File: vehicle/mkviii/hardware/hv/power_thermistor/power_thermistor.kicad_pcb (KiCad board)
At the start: 4 copper layers, 401 x 176.1 mm, 97 parts, among them J10 Battery Cell Spot Weld, J11 Battery Cell Spot Weld, J12 Battery Cell Spot Weld, J13 Battery Cell Spot Weld, J14 Battery Cell Spot Weld, J15 Battery Cell Spot Weld, J16 Battery Cell Spot Weld, J17 Battery Cell Spot Weld, J18 Battery Cell Spot Weld, J19 Battery Cell Spot Weld, J2 43045-02YY_121314, J2 EHT-110-01-F-D, J20 Battery Cell Spot Weld, J3 EHT-110-01-F-D, J5 Battery Cell Spot Weld, J6 Battery Cell Spot Weld, J6 EHT-110-01-F-D, J7 Battery Cell Spot Weld, J8 Battery Cell Spot Weld, J9 Battery Cell Spot Weld

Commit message: Added Production Files and updated PCB file to match PCB file used for production files.
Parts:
- added kibuzzard-69840B33: G***, kibuzzard-69840B33, F.Cu at (71.2, 32.4)
- added kibuzzard-69840B56: G***, kibuzzard-69840B56, F.Cu at (74.3, 35.2)
- added kibuzzard-69840BF2: G***, kibuzzard-69840BF2, F.Cu at (224.3, 35.0)
- added kibuzzard-69840BF7: G***, kibuzzard-69840BF7, F.Cu at (224.1, 37.6)
- added kibuzzard-69840C1E: G***, kibuzzard-69840C1E, F.Cu at (297.1, 37.8)
- added kibuzzard-69840C4F: G***, kibuzzard-69840C4F, F.Cu at (298.9, 35.2)
- added kibuzzard-69840C62: G***, kibuzzard-69840C62, F.Cu at (342.2, 37.8)
- added kibuzzard-69840C71: G***, kibuzzard-69840C71, F.Cu at (343.5, 35.2)
- moved kibuzzard-6738FB72 2.18 mm to (327.2, 36.5)
- moved kibuzzard-6738FB72 0.67 mm to (282.6, 36.5)
- moved kibuzzard-6738FA22 0.35 mm to (210.4, 36.5)
- renumbered REF** to U1
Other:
- board text removed: "02/2026"
- board text removed: "Liam Fries"

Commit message: Power Therm overhall, have not been reviewed yet
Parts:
- removed the J2 at (185.0, 27.7)
- removed the J2 at (216.2, 29.1)
- added J1: T2M-110-01-X-D-TH-WT, OEM:SAMTEC_EHT-110-01-X-D (J_EHT-110-01-F-D), B.Cu at (290.3, 29.0)
- added J2: J_Molex_Header_01x02_VT, OEM:J_Molex_Header_01x02_VT - 43045-02YY_121314, B.Cu at (161.9, 30.4)
- added J20: Battery Cell Spot Weld, OEM:J_Bond_Pad_4p, F.Cu at (-10.3, 26.7)
- added J23: Battery Cell Spot Weld, OEM:J_Bond_Pad_4p, F.Cu at (-0.81, 26.7)
- added J4: T2M-110-01-X-D-TH-WT, OEM:SAMTEC_EHT-110-01-X-D (J_EHT-110-01-F-D), B.Cu at (216.1, 29.0)
- added kibuzzard-6738FA22: G***, kibuzzard-6738FA22, F.Cu at (210.4, 36.5)
- added kibuzzard-6738FB72: G***, kibuzzard-6738FB72, B.Cu at (298.3, 36.4)
- added kibuzzard-6738FB72: G***, kibuzzard-6738FB72, B.Cu at (345.5, 36.5)
- added kibuzzard-69840BF2: G***, kibuzzard-69840BF2, F.Cu at (224.3, 35.0)
- added kibuzzard-69840BF7: G***, kibuzzard-69840BF7, F.Cu at (224.1, 37.6)
- added kibuzzard-69840C1E: G***, kibuzzard-69840C1E, B.Cu at (283.9, 37.8)
- added kibuzzard-69840C4F: G***, kibuzzard-69840C4F, B.Cu at (282.0, 35.2)
- added kibuzzard-69840C62: G***, kibuzzard-69840C62, B.Cu at (330.6, 37.9)
- added kibuzzard-69840C71: G***, kibuzzard-69840C71, B.Cu at (329.3, 35.3)
- J19: renamed from J2; value (none) -> Battery Cell Spot Weld
- J3: value EHT-110-01-F-D -> T2M-110-01-X-D-TH-WT; moved to B.Cu
- J6: value EHT-110-01-F-D -> J_Molex_Header_01x02_VT; footprint OEM:SAMTEC_EHT-110-01-X-D (J_EHT-110-01-F-D) -> OEM:J_Molex_Header_01x02_VT - 43045-02YY_121314; moved to B.Cu
- REF** (x2), kibuzzard-6738FA22, kibuzzard-69840BF2, kibuzzard-69840BF7: moved to B.Cu
- U1: value 21-0036K_MXM -> DS18B20U
- moved TH1 319.3 mm to (56.4, 106.0)
- moved TH2 319.3 mm to (56.4, 159.7)
- moved J6 75.0 mm to (365.2, 30.4)
- moved TH18 24.0 mm to (229.6, 160.0), turned to 90 degrees
- moved TH21 21.8 mm to (270.0, 105.9)
- moved TH22 21.8 mm to (270.0, 159.8)
- moved TH10 21.7 mm to (142.0, 159.8)
- moved TH9 21.7 mm to (142.0, 105.9)
- moved TH3 21.5 mm to (77.9, 92.5)
- moved TH4 21.5 mm to (77.9, 146.4)
- moved TH19 21.5 mm to (248.4, 92.4)
- moved TH27 21.4 mm to (333.6, 92.5)
- moved TH28 21.4 mm to (333.6, 146.4)
- moved TH23 21.3 mm to (290.8, 92.5)
- moved TH24 21.3 mm to (290.8, 146.4)
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- renumbered J12 to J10, J13 to J11, J14 to J12, J15 to J13, J16 to J14, J17 to J15, J18 to J16, J19 to J17, J7 to J18, J20 to J22, J8 to J5, J9 to J50, J6 to J51, J5 to J7, J10 to J8, J11 to J9, TH31 to TH1, TH8 to TH10, TH9 to TH11, TH10 to TH12, TH11 to TH13, TH12 to TH14, TH13 to TH15, TH14 to TH16, TH15 to TH17, TH16 to TH18, TH17 to TH19, TH32 to TH2, TH18 to TH20, TH19 to TH21, TH20 to TH22, TH21 to TH23, TH22 to TH24, TH23 to TH25, TH24 to TH26, TH25 to TH27, TH26 to TH28, TH27 to TH29, TH1 to TH3, TH28 to TH30, TH29 to TH31, TH30 to TH32, TH2 to TH4, TH3 to TH5, TH4 to TH6, TH5 to TH7, TH6 to TH8, TH7 to TH9
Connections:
- F5 pad 1: Net-(JP1-B) -> Net-(JP9-B)
- J3 pad 01: Therm18 -> GND
- J3 pad 02: unconnected-(J3-Pad02) -> Therm17
- J3 pad 03: Therm19 -> Therm31
- J3 pad 04: Therm17 -> Therm18
- J3 pad 05: GND -> Therm32
- J3 pad 06: Therm32 -> GND
- J3 pad 07: Therm20 -> Therm29
- J3 pad 08: Therm31 -> Therm20
- J3 pad 09: Therm21 -> GND
- J3 pad 10: GND -> Therm19
- J3 pad 11: Therm22 -> Therm30
- J3 pad 12: Therm30 -> Therm22
- J3 pad 13: Therm23 -> Therm27
- J3 pad 14: Therm29 -> Therm21
- J3 pad 15: GND -> Therm28
- J3 pad 16: Therm28 -> GND
- J3 pad 17: Therm24 -> Therm25
- J3 pad 18: Therm27 -> Therm24
- J3 pad 19: Therm25 -> Therm26
- J3 pad 20: Therm26 -> Therm23
- JP9 pad 2: Net-(JP1-B) -> Net-(JP9-B)
- TH1 pad 2: Therm31 -> Therm1
- TH10 pad 2: Therm8 -> Therm10
- TH11 pad 2: Therm9 -> Therm11
- TH12 pad 2: Therm10 -> Therm12
- TH13 pad 2: Therm11 -> Therm13
- TH14 pad 2: Therm12 -> Therm14
- TH15 pad 2: Therm13 -> Therm15
- TH16 pad 2: Therm14 -> Therm16
- TH17 pad 2: Therm15 -> Therm17
- TH18 pad 2: Therm16 -> Therm18
- TH19 pad 2: Therm17 -> Therm19
- TH2 pad 2: Therm32 -> Therm2
- TH20 pad 2: Therm18 -> Therm20
- TH21 pad 2: Therm19 -> Therm21
- TH22 pad 2: Therm20 -> Therm22
- TH23 pad 2: Therm21 -> Therm23
- TH24 pad 2: Therm22 -> Therm24
- TH25 pad 2: Therm23 -> Therm25
- TH26 pad 2: Therm24 -> Therm26
- TH27 pad 2: Therm25 -> Therm27
- TH28 pad 2: Therm26 -> Therm28
- TH29 pad 2: Therm27 -> Therm29
- TH3 pad 2: Therm1 -> Therm3
- TH30 pad 2: Therm28 -> Therm30
- TH31 pad 2: Therm29 -> Therm31
- TH32 pad 2: Therm30 -> Therm32
- TH4 pad 2: Therm2 -> Therm4
- TH5 pad 2: Therm3 -> Therm5
- TH6 pad 2: Therm4 -> Therm6
- TH7 pad 2: Therm5 -> Therm7
- TH8 pad 2: Therm6 -> Therm8
- TH9 pad 2: Therm7 -> Therm9
- U1 pad 1: unconnected-(J2-Pad18) -> Net-(U1-DQ)
- U1 pad 2: (no net) -> unconnected-(U1-NC-Pad2)
- U1 pad 3: (no net) -> unconnected-(U1-NC-Pad3)
- U1 pad 4: unconnected-(J2-Pad19) -> Net-(U1-GND)
- U1 pad 5: (no net) -> unconnected-(U1-NC-Pad5)
- U1 pad 6: (no net) -> unconnected-(U1-NC-Pad6)
- U1 pad 7: (no net) -> unconnected-(U1-NC-Pad7)
- U1 pad 8: unconnected-(J2-Pad19) -> Net-(U1-GND)
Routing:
- net Net-(U1-GND): track 0.00 -> 365.0 mm, vias 0 -> 2
- net Net-(U1-DQ): track 0.00 -> 333.6 mm, vias 0 -> 3
- net unconnected-(J2-Pad18): track 164.5 -> 0.00 mm, vias 2 -> 0
- net unconnected-(J2-Pad19): track 152.8 -> 0.00 mm, vias 2 -> 0
- net Therm15: track 227.3 -> 150.8 mm
- net Therm11: track 254.2 -> 181.5 mm
- net Therm12: track 294.5 -> 240.5 mm
- net Therm16: track 267.4 -> 216.3 mm
- net Therm9: track 254.8 -> 206.0 mm
- net Therm13: track 226.1 -> 177.9 mm
- net CELL4: track 197.4 -> 154.5 mm
- net CELL5: track 173.4 -> 132.4 mm
- net CELL3: track 221.5 -> 181.0 mm
- net Therm14: track 268.9 -> 232.2 mm
- net CELL6: track 149.1 -> 114.4 mm
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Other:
- board size 401 x 176.1 mm -> 400.9 x 174.3 mm

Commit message: fixed suggested edits and moved connector
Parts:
- removed J20, J23: Battery Cell Spot Weld, OEM:J_Bond_Pad_4p
- removed kibuzzard-69840B33: G***, kibuzzard-69840B33
- removed kibuzzard-69840B56: G***, kibuzzard-69840B56
- added kibuzzard-69DFA9BC: G***, kibuzzard-69DFA9BC, F.Cu at (79.0, 35.2)
- added kibuzzard-69DFAA3E: G***, kibuzzard-69DFAA3E, F.Cu at (74.3, 38.1)
- added kibuzzard-69E00A54: G***, kibuzzard-69E00A54, B.Cu at (104.8, 31.9)
- added kibuzzard-69E00A54: G***, kibuzzard-69E00A54, B.Cu at (270.4, 32.2)
- moved J6 95.3 mm to (270.2, 23.6)
- moved J2 57.7 mm to (104.6, 23.6)
- moved J3 9.44 mm to (344.3, 25.3)
- moved kibuzzard-6738FA22 9.44 mm to (229.9, 32.6)
- moved kibuzzard-69840C1E 9.44 mm to (292.5, 34.0)
- moved kibuzzard-69840C4F 9.44 mm to (307.5, 31.4)
- moved kibuzzard-69840C62 9.44 mm to (339.2, 34.1)
- moved kibuzzard-69840C71 9.44 mm to (352.1, 31.4)
- moved kibuzzard-69840C71 9.44 mm to (337.9, 31.5)
- moved kibuzzard-69840C1E 9.44 mm to (305.7, 34.0)
- moved kibuzzard-69840C4F 9.44 mm to (290.7, 31.4)
- moved kibuzzard-69840C62 9.44 mm to (350.8, 34.0)
- moved kibuzzard-6738FA22 9.44 mm to (219.0, 32.6)
- moved kibuzzard-69840BF7 9.44 mm to (232.7, 33.8)
- moved kibuzzard-69840BF7 9.44 mm to (216.2, 33.8)
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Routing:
- net Net-(U1-GND): track 365.0 -> 300.9 mm, vias 2 -> 1
- net Net-(U1-DQ): track 333.6 -> 298.6 mm, vias 3 -> 4
- net Therm18: track 205.1 -> 216.6 mm
- net Therm19: track 139.7 -> 151.2 mm
- net Therm21: track 131.6 -> 142.9 mm
- net Therm22: track 194.1 -> 205.3 mm
- net Therm20: track 197.4 -> 208.6 mm
- net Therm17: track 160.0 -> 171.0 mm
- net CELL16: track 248.3 -> 237.7 mm
- net Therm24: track 169.3 -> 180.0 mm
- net Therm23: track 107.3 -> 117.9 mm
- net Therm10: track 267.9 -> 278.4 mm
- net CELL10: track 120.1 -> 109.8 mm
- net Therm9: track 206.0 -> 216.2 mm
- net CELL5: track 132.4 -> 142.6 mm
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
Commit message: Minor redcube schematic changes; added some silkscreen; added production files
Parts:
- removed kibuzzard-69DFAA3E: G***, kibuzzard-69DFAA3E
- added G***: LOGO, LOGO, B.Cu at (74.1, 37.6)
- added REF**: OEM_Logo_8mm, OEM:OEM_Logo_8mm, B.Cu at (94.4, 24.4)
- added kibuzzard-67390047: G***, kibuzzard-67390047, B.Cu at (82.7, 21.6)
- added kibuzzard-69DFA9BC: G***, kibuzzard-69DFA9BC, B.Cu at (76.4, 24.4)
- added kibuzzard-69E00A54: G***, kibuzzard-69E00A54, F.Cu at (270.4, 32.2)
- added kibuzzard-69E00A54: G***, kibuzzard-69E00A54, F.Cu at (104.8, 31.9)
- added kibuzzard-69E05987: G***, kibuzzard-69E05987, F.Cu at (80.2, 27.3)
- added kibuzzard-69E05987: G***, kibuzzard-69E05987, B.Cu at (81.1, 27.3)
- J20, J23: renamed from REF**; value J_Wurth_7461115 -> J_Redcube
- moved kibuzzard-6739182D 66.3 mm to (174.7, 24.8)
- moved G*** 13.9 mm to (74.4, 37.4)
- moved REF** 12.3 mm to (66.9, 24.4)
- moved kibuzzard-67390047 12.3 mm to (78.7, 21.6)
- moved kibuzzard-69DFA9BC 12.3 mm to (84.9, 24.4)
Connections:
- J1 pad 13: Therm3 -> Therm4
- J1 pad 15: Therm4 -> Therm3
- J4 pad 01: CELL4 -> CELL1
- J4 pad 02: CELL5 -> CELL16
- J4 pad 03: CELL3 -> CELL2
- J4 pad 04: CELL6 -> CELL15
- J4 pad 05: CELL2 -> CELL3
- J4 pad 06: CELL7 -> CELL14
- J4 pad 07: CELL1 -> CELL4
- J4 pad 08: CELL8 -> CELL13
- J4 pad 09: CELL16 -> CELL5
- J4 pad 10: CELL9 -> CELL12
- J4 pad 11: CELL15 -> CELL6
- J4 pad 12: CELL10 -> CELL11
- J4 pad 13: CELL14 -> CELL7
- J4 pad 14: CELL11 -> CELL10
- J4 pad 16: CELL12 -> CELL9
- J4 pad 18: CELL13 -> CELL8
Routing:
- added copper zone on B.Cu, net (none)
- added copper zone on F.Cu, net (none)
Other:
- board text added: "+"
- board text added: "-"
- board text added: "0"
- board text added: "1"
- board text added: "10"
- board text added: "11"
- board text added: "12"
- board text added: "13"
- board text added: "14"
- board text added: "15"
- board text added: "16"
- board text added: "2"
- board text added: "3"
- board text added: "4"
- board text added: "5"
- board text added: "6"
- board text added: "7"
- board text added: "8"
- board text added: "9"

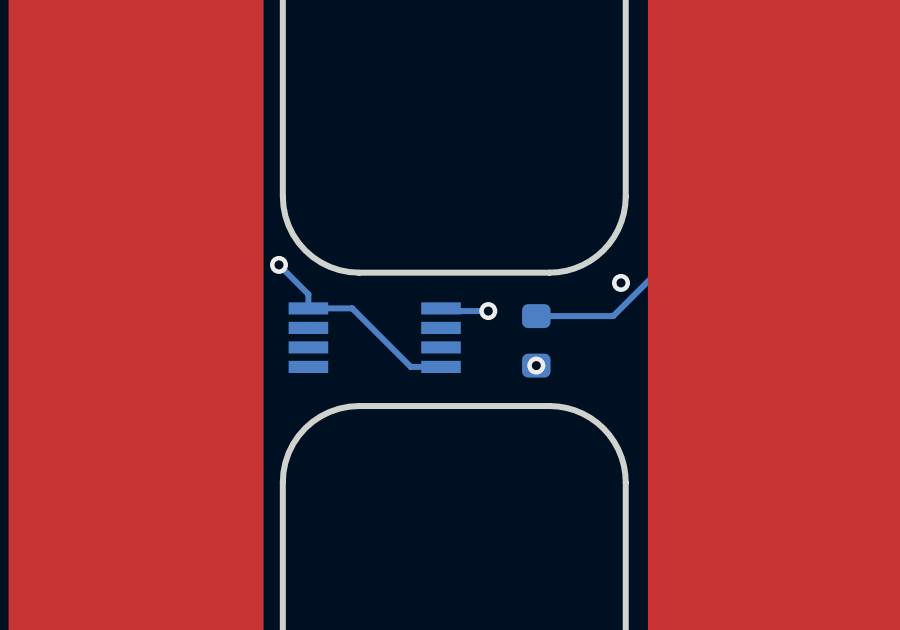
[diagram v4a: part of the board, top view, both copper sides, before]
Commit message: moved e-meter part and moved up GND plane
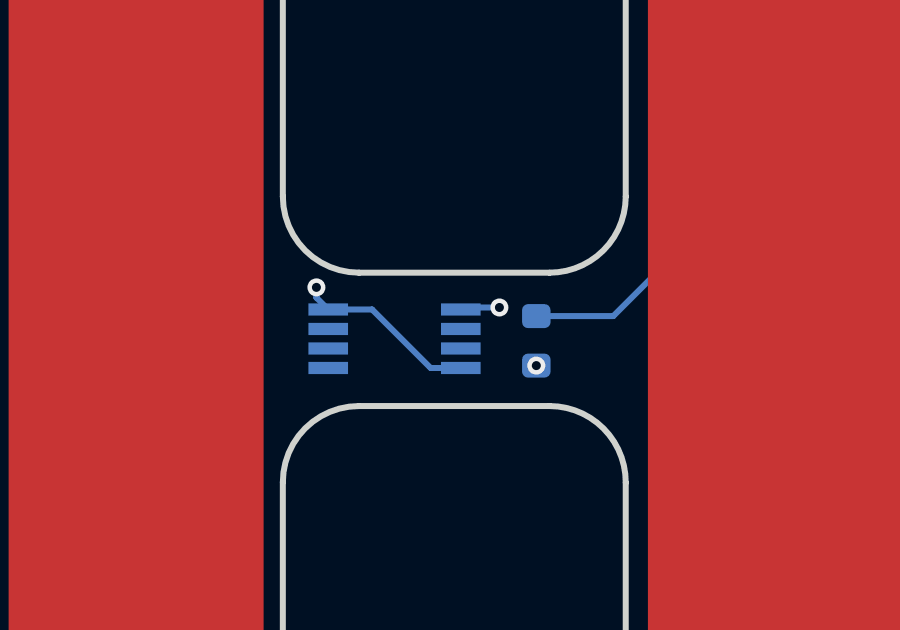
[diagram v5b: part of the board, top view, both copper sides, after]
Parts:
- moved U1 0.66 mm to (224.9, 159.9)
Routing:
- net Net-(U1-GND): track 300.9 -> 301.5 mm
- net Net-(U1-DQ): track 298.6 -> 298.0 mm, vias 4 -> 3
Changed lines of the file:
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@@
 	(footprint "OEM:8-uSOP"
 		(layer "B.Cu")
-		(at 224.193089 159.846006 180)
+		(at 224.853386 159.881568 180)
 		(tags "DS18B20U")
 		(property "Reference" "U1"
@@
 	)
 	(via
-		(at 221.002889 157.421366)
+		(at 222.25 158.17)
 		(size 0.6)
 		(drill 0.3)
 		(layers "F.Cu" "B.Cu")
-		(free yes)
 		(net 68)
 	)
 	(segment
-		(start 226.402889 160.821366)
-		(end 225.396489 160.821366)
+		(start 222.25 158.512622)
+		(end 222.643586 158.906208)
 		(width 0.2)
 		(layer "B.Cu")
@@
 	)
 	(segment
-		(start 225.396489 160.821366)
-		(end 223.445769 158.870646)
+		(start 227.063186 160.856928)
+		(end 226.056786 160.856928)
 		(width 0.2)
 		(layer "B.Cu")
@@
 	)
 	(segment
-		(start 221.983289 158.870646)
-		(end 221.983289 158.401766)
+		(start 226.056786 160.856928)
+		(end 224.106066 158.906208)
 		(width 0.2)
 		(layer "B.Cu")
@@
 	)
 	(segment
-		(start 223.445769 158.870646)
-		(end 221.983289 158.870646)
+		(start 222.25 158.17)
+		(end 222.25 158.512622)
 		(width 0.2)
 		(layer "B.Cu")
@@
 	)
 	(segment
-		(start 221.983289 158.401766)
-		(end 221.002889 157.421366)
+		(start 224.106066 158.906208)
+		(end 222.643586 158.906208)
 		(width 0.2)
 		(layer "B.Cu")
@@
 	)
 	(segment
+		(start 221.751523 158.17)
+		(end 222.25 158.17)
+		(width 0.2)
+		(layer "In1.Cu")
+		(net 68)
+	)
+	(segment
 		(start 220.5 63.56)
 		(end 220.55 63.56)
@@
 	)
 	(segment
-		(start 221.002889 157.421366)
-		(end 220.5 156.918477)
+		(start 220.5 156.918477)
+		(end 221.751523 158.17)
 		(width 0.2)
 		(layer "In1.Cu")
@@
 	)
 	(via
-		(at 227.98 158.96)
-		(size 0.6)
-		(drill 0.3)
-		(layers "F.Cu" "B.Cu")
-		(net 69)
-	)
-	(via
 		(at 221.68 65.53)
 		(size 0.6)
@@
 	)
 	(via
-		(at 232.402889 158.021366)
+		(at 228.35 158.84)
 		(size 0.6)
 		(drill 0.3)
 		(layers "F.Cu" "B.Cu")
-		(free yes)
 		(net 69)
 	)
@@
 	)
 	(segment
-		(start 221.68 65.53)
-		(end 220.3 65.53)
+		(start 227.129394 158.84)
+		(end 227.063186 158.906208)
+		(width 0.2)
+		(layer "B.Cu")
+		(net 69)
+	)
+	(segment
+		(start 228.35 158.84)
+		(end 227.129394 158.84)
 		(width 0.2)
 		(layer "B.Cu")
@@
 	)
 	(segment
-		(start 227.98 158.96)
-		(end 226.492243 158.96)
+		(start 221.68 65.53)
+		(end 220.3 65.53)
 		(width 0.2)
 		(layer "B.Cu")
@@
 	)
 	(segment
-		(start 226.492243 158.96)
-		(end 226.402889 158.870646)
+		(start 227.15254 158.995562)
+		(end 227.063186 158.906208)
 		(width 0.2)
 		(layer "B.Cu")
@@
 	)
 	(segment
-		(start 198.47 44.3)
-		(end 122.28 44.3)
+		(start 233.6 156.824255)
+		(end 231.584255 158.84)
 		(width 0.2)
 		(layer "In1.Cu")
@@
 	)
 	(segment
-		(start 233.6 65.63)
-		(end 233.6 156.824255)
+		(start 198.47 44.3)
+		(end 122.28 44.3)
 		(width 0.2)
 		(layer "In1.Cu")
@@
 	)
 	(segment
-		(start 231.464255 158.96)
-		(end 227.98 158.96)
+		(start 233.6 65.63)
+		(end 233.6 156.824255)
 		(width 0.2)
 		(layer "In1.Cu")
@@
 	)
 	(segment
-		(start 232.402889 158.021366)
-		(end 231.464255 158.96)
-		(width 0.2)
-		(layer "In1.Cu")
-		(net 69)
-	)
-	(segment
-		(start 233.6 156.824255)
-		(end 232.402889 158.021366)
+		(start 231.584255 158.84)
+		(end 228.35 158.84)
 		(width 0.2)
 		(layer "In1.Cu")
@@
 		(polygon
 			(pts
-				(xy 52.4 177.059668) (xy 51.7 15.726694) (xy 371 15.533938) (xy 371.7 176.96)
+				(xy 52.7 162.509668) (xy 51.7 15.726694) (xy 371 15.533938) (xy 372 162.41)
 			)
 		)

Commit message: fixes for connector to BMS MOBO
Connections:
- J1 pad 01: GND -> Therm7
- J1 pad 02: Therm10 -> unconnected-(J1-Pad02)
- J1 pad 03: Therm7 -> Therm8
- J1 pad 04: Therm9 -> Therm10
- J1 pad 05: Therm8 -> GND
- J1 pad 06: GND -> Therm9
- J1 pad 09: GND -> Therm6
- J1 pad 10: Therm11 -> GND
- J1 pad 11: Therm6 -> Therm3
- J1 pad 12: Therm14 -> Therm11
- J1 pad 14: Therm13 -> Therm14
- J1 pad 15: Therm3 -> GND
- J1 pad 16: GND -> Therm13
- J3 pad 01: GND -> Therm31
- J3 pad 02: Therm17 -> unconnected-(J3-Pad02)
- J3 pad 03: Therm31 -> Therm32
- J3 pad 04: Therm18 -> Therm17
- J3 pad 05: Therm32 -> GND
- J3 pad 06: GND -> Therm18
- J3 pad 09: GND -> Therm30
- J3 pad 10: Therm19 -> GND
- J3 pad 11: Therm30 -> Therm27
- J3 pad 12: Therm22 -> Therm19
- J3 pad 13: Therm27 -> Therm28
- J3 pad 14: Therm21 -> Therm22
- J3 pad 15: Therm28 -> GND
- J3 pad 16: GND -> Therm21
- J4 pad 01: CELL1 -> CELL8
- J4 pad 02: CELL16 -> CELL7
- J4 pad 03: CELL2 -> CELL9
- J4 pad 04: CELL15 -> CELL6
- J4 pad 05: CELL3 -> CELL10
- J4 pad 06: CELL14 -> CELL5
- J4 pad 07: CELL4 -> CELL11
- J4 pad 08: CELL13 -> CELL4
- J4 pad 09: CELL5 -> CELL12
- J4 pad 10: CELL12 -> CELL3
- J4 pad 11: CELL6 -> CELL13
- J4 pad 12: CELL11 -> CELL2
- J4 pad 13: CELL7 -> CELL14
- J4 pad 14: CELL10 -> CELL1
- J4 pad 15: GND -> CELL15
- J4 pad 16: CELL9 -> GND
- J4 pad 17: unconnected-(J4-Pad17) -> CELL16
- J4 pad 18: CELL8 -> unconnected-(J4-Pad18)
- J4 pad 20: GND -> unconnected-(J4-Pad20)
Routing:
- net CELL9: track 101.1 -> 127.7 mm, vias 0 -> 1
- net CELL10: track 109.8 -> 130.9 mm, vias 0 -> 1
- net CELL11: track 129.1 -> 147.1 mm, vias 0 -> 1
- net CELL12: track 148.4 -> 161.5 mm, vias 0 -> 1
- net CELL13: track 167.7 -> 179.3 mm, vias 0 -> 1
- net CELL16: track 237.7 -> 228.5 mm
- net CELL4: track 164.7 -> 169.9 mm, vias 0 -> 1
- net CELL15: track 219.3 -> 214.5 mm, vias 0 -> 1
- net CELL5: track 142.6 -> 147.0 mm, vias 0 -> 1
- net CELL3: track 189.2 -> 193.2 mm, vias 0 -> 1
- net CELL8: track 98.6 -> 102.0 mm
- net CELL2: track 213.2 -> 216.4 mm, vias 0 -> 1
- net CELL1: track 236.6 -> 239.7 mm, vias 0 -> 1
- net Therm14: track 241.5 -> 244.6 mm
- net Therm10: track 278.4 -> 280.5 mm
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
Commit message: fixed a trace
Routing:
- net Net-(U1-DQ): track 298.0 -> 298.9 mm
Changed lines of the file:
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@@
 	)
 	(segment
-		(start 233.6 156.824255)
-		(end 231.584255 158.84)
+		(start 233.6 65.63)
+		(end 270.21 29.02)
 		(width 0.2)
 		(layer "In1.Cu")
@@
 	)
 	(segment
-		(start 233.6 65.63)
+		(start 221.68 65.53)
+		(end 221.78 65.63)
+		(width 0.2)
+		(layer "In1.Cu")
+		(net 69)
+	)
+	(segment
+		(start 233.6 67.75)
 		(end 233.6 156.824255)
+		(width 0.2)
+		(layer "In1.Cu")
+		(net 69)
+	)
+	(segment
+		(start 221.78 65.63)
+		(end 231.48 65.63)
+		(width 0.2)
+		(layer "In1.Cu")
+		(net 69)
+	)
+	(segment
+		(start 231.48 65.63)
+		(end 233.6 67.75)
+		(width 0.2)
+		(layer "In1.Cu")
+		(net 69)
+	)
+	(segment
+		(start 231.584255 158.84)
+		(end 228.35 158.84)
 		(width 0.2)
 		(layer "In1.Cu")
@@
 	)
 	(segment
-		(start 233.6 65.63)
-		(end 270.21 29.02)
+		(start 233.6 67.75)
+		(end 233.6 65.63)
 		(width 0.2)
 		(layer "In1.Cu")
@@
 	)
 	(segment
-		(start 233.6 65.63)
-		(end 221.78 65.63)
-		(width 0.2)
-		(layer "In1.Cu")
-		(net 69)
-	)
-	(segment
-		(start 231.584255 158.84)
-		(end 228.35 158.84)
+		(start 233.6 156.824255)
+		(end 231.584255 158.84)
 		(width 0.2)
 		(layer "In1.Cu")
@@
 		(width 0.2)
 		(layer "In1.Cu")
-		(net 69)
-	)
-	(segment
-		(start 221.78 65.63)
-		(end 221.68 65.53)
-		(width 0.2)
-		(layer "In1.Cu")
